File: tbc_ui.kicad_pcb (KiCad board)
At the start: 2 copper layers, 160 x 50 mm, 30 parts, among them J1 75869-105LF, SW1 PEC11R-4220F-S0024, U1 CD74HC14M96

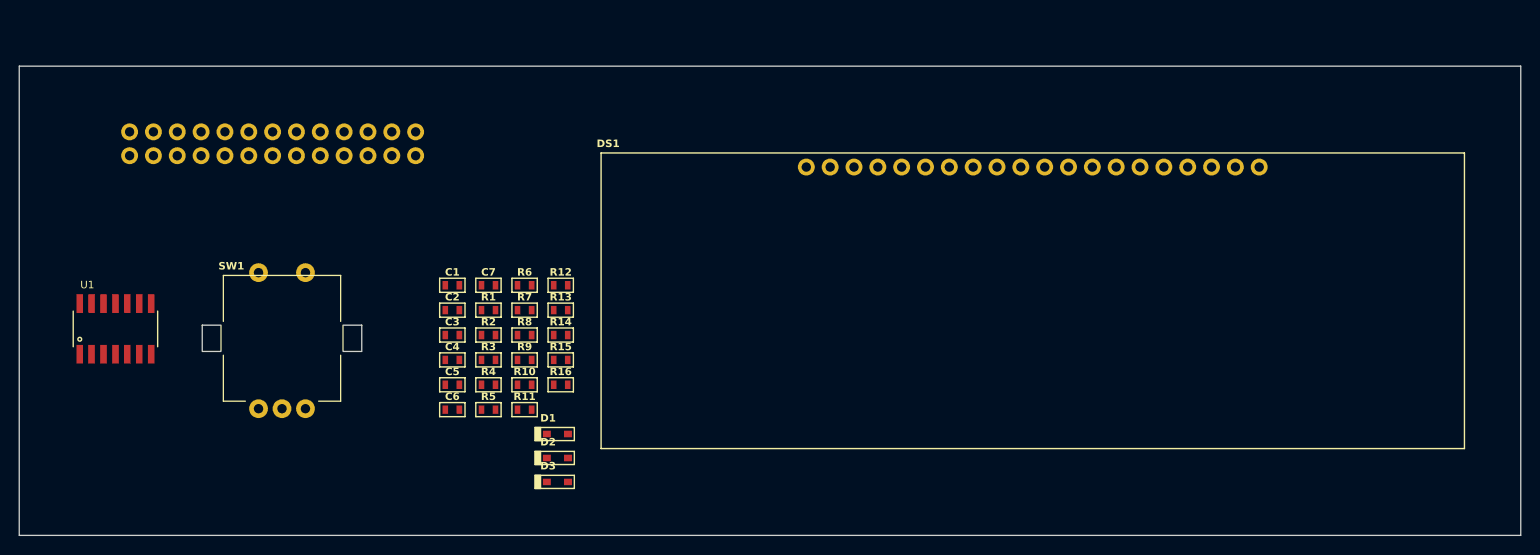
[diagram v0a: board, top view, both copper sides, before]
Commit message: additional footprints and layout
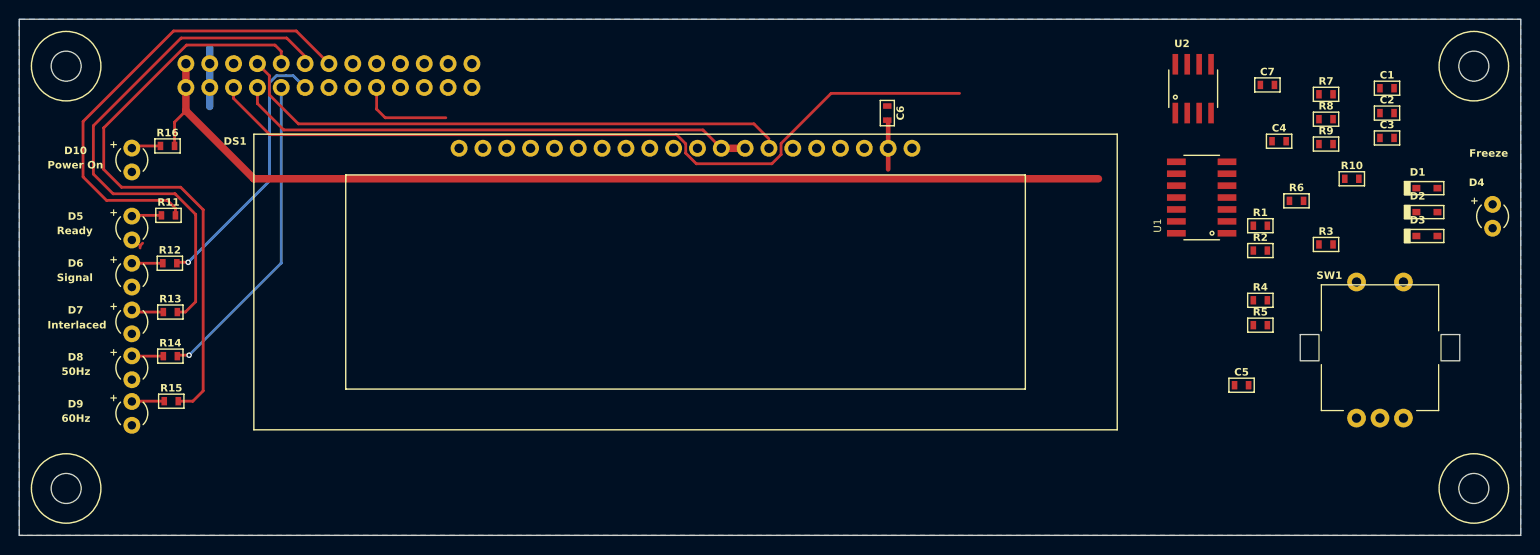
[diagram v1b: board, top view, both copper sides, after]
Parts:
- added D10: WP424NDT, tbc-ui:WP424, F.Cu at (92.0, 80.0)
- added D4: WP424IDT, tbc-ui:WP424, F.Cu at (237.0, 86.0)
- added D5: WP424GDT, tbc-ui:WP424, F.Cu at (92.0, 87.2)
- added D6: WP424GDT, tbc-ui:WP424, F.Cu at (92.0, 92.3)
- added D7: WP424GDT, tbc-ui:WP424, F.Cu at (92.0, 97.2)
- added D8: WP424GDT, tbc-ui:WP424, F.Cu at (92.0, 102.1)
- added D9: WP424GDT, tbc-ui:WP424, F.Cu at (92.0, 107.0)
- added MH1: MH_7.4MMNCx3.2MMD, tbc-ui:MH_7.4MMCx3.2MMD_NON_COPPER_NPTH, F.Cu at (85.0, 70.0)
- added MH2: MH_7.4MMNCx3.2MMD, tbc-ui:MH_7.4MMCx3.2MMD_NON_COPPER_NPTH, F.Cu at (85.0, 115.0)
- added MH3: MH_7.4MMNCx3.2MMD, tbc-ui:MH_7.4MMCx3.2MMD_NON_COPPER_NPTH, F.Cu at (235.0, 70.0)
- added MH4: MH_7.4MMNCx3.2MMD, tbc-ui:MH_7.4MMCx3.2MMD_NON_COPPER_NPTH, F.Cu at (235.0, 115.0)
- added U2: ICM7555CBAZ, tbc-ui:SOIC-8, F.Cu at (205.1, 72.4)
- moved SW1 117.0 mm to (225.0, 100.0)
- moved U1 116.6 mm to (206.0, 84.0), turned to 90 degrees
- moved C1 101.8 mm to (225.8, 72.3)
- moved C2 101.8 mm to (225.8, 75.0)
- moved C3 101.8 mm to (225.8, 77.7)
- moved D1 96.3 mm to (230.0, 83.0)
- moved D2 96.3 mm to (230.0, 85.5)
- moved D3 96.3 mm to (230.0, 88.1)
- moved C4 91.1 mm to (214.2, 78.0)
- moved R10 90.8 mm to (222.0, 82.0)
- moved R3 90.1 mm to (219.2, 89.0)
- moved R7 88.4 mm to (219.2, 73.0)
- moved R8 88.4 mm to (219.2, 75.7)
- moved R9 88.4 mm to (219.2, 78.3)
- moved C7 85.7 mm to (213.0, 72.0)
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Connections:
- DS1 pad 1: (no net) -> GND
- DS1 pad 10: (no net) -> GND
- DS1 pad 11: (no net) -> GND
- DS1 pad 12: (no net) -> GND
- DS1 pad 13: (no net) -> GND
- DS1 pad 14: (no net) -> GND
- DS1 pad 15: (no net) -> GND
- DS1 pad 16: (no net) -> +3V3
- DS1 pad 17: (no net) -> GND
- DS1 pad 18: (no net) -> +3V3
- DS1 pad 19: (no net) -> GND
- DS1 pad 2: (no net) -> +3V3
- DS1 pad 20: (no net) -> GND
- DS1 pad 3: (no net) -> GND
- DS1 pad 4: (no net) -> GND
- DS1 pad 5: (no net) -> GND
- DS1 pad 6: (no net) -> GND
- DS1 pad 7: (no net) -> /SCL
- DS1 pad 8: (no net) -> /SDA
- DS1 pad 9: (no net) -> /SDA
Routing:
- net +3V3: track 0.00 -> 115.2 mm
- net /FREEZE: track 0.00 -> 85.8 mm
- net /D_60HZ: track 0.00 -> 63.4 mm
- net /SCL: track 0.00 -> 59.0 mm
- net /D_INTERLACED: track 0.00 -> 58.2 mm
- net /SDA: track 0.00 -> 55.7 mm
- net /D_READY: track 0.00 -> 49.5 mm
- net /D_50HZ: track 0.00 -> 33.9 mm, vias 0 -> 1
- net /D_SIGNAL: track 0.00 -> 28.6 mm, vias 0 -> 1
- net /RENC_B: track 0.00 -> 10.1 mm
- net GND: track 0.00 -> 6.25 mm
- net Net-(D9-Anode): track 0.00 -> 3.46 mm
- net Net-(D7-Anode): track 0.00 -> 3.44 mm
- net Net-(D8-Anode): track 0.00 -> 3.36 mm
- net Net-(D6-Anode): track 0.00 -> 3.30 mm
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- added copper zone on B.Cu, net GND
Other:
- board size 160 x 50 mm -> 160 x 55 mm

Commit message: updated to Kicad 8, finished footprints and layouts, erc passed
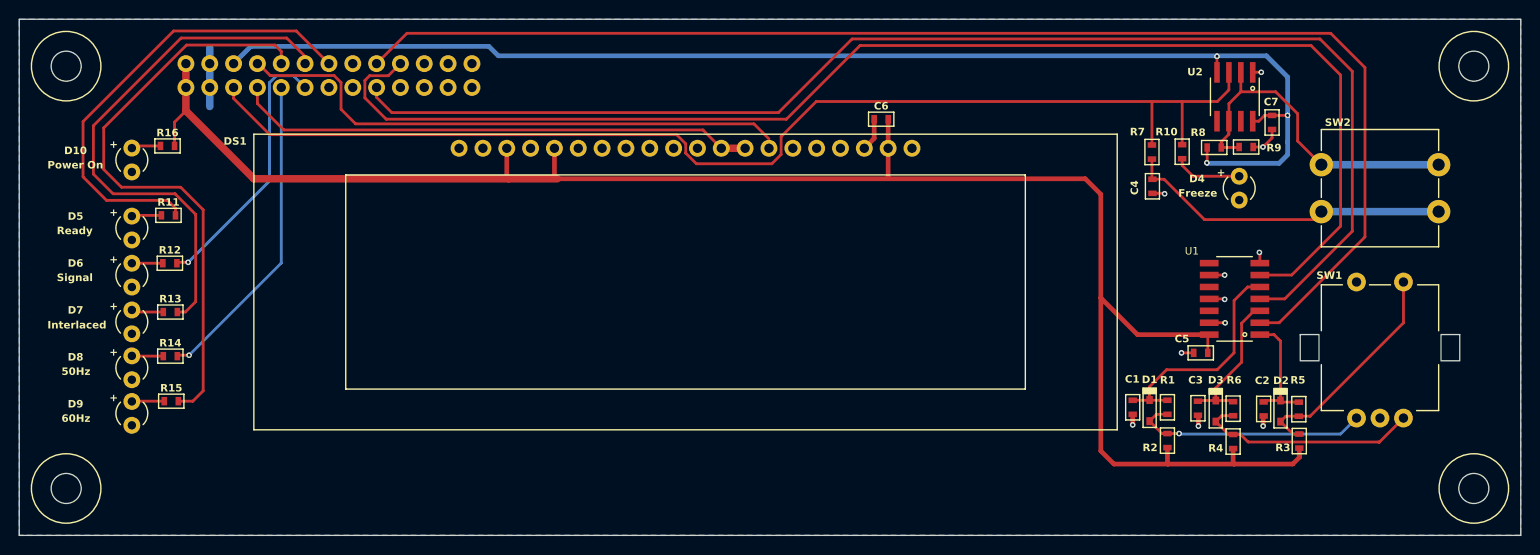
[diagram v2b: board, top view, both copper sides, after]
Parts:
- added SW2: TL1100F160Q, tbc-ui:TL1100F, F.Cu at (225.0, 83.0)
- moved C1 43.5 mm to (198.7, 106.3), turned to 90 degrees
- moved D1 37.9 mm to (200.4, 106.7), turned to -90 degrees
- moved C3 35.1 mm to (205.6, 106.5), turned to 90 degrees
- moved C2 34.2 mm to (212.6, 106.5), turned to 90 degrees
- moved D3 29.2 mm to (207.5, 106.8), turned to -90 degrees
- moved D4 27.2 mm to (210.0, 83.0)
- moved D2 26.3 mm to (214.4, 106.8), turned to -90 degrees
- moved R6 23.2 mm to (209.3, 106.5), turned to -90 degrees
- moved R2 22.5 mm to (202.3, 109.9), turned to 90 degrees
- moved R1 21.7 mm to (202.3, 106.3), turned to -90 degrees
- moved R3 21.1 mm to (216.4, 110.0), turned to -90 degrees
- moved R7 19.5 mm to (200.7, 79.2), turned to 90 degrees
- moved R10 18.3 mm to (203.9, 79.1), turned to 90 degrees
- moved R4 15.3 mm to (209.3, 110.0), turned to -90 degrees
- moved C4 14.3 mm to (200.8, 82.8), turned to 90 degrees
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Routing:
- net /RENC_A: track 0.00 -> 142.7 mm
- net /RENC_SW: track 0.00 -> 141.2 mm
- net +5V: track 0.00 -> 139.1 mm, vias 0 -> 3
- net /RENC_B: track 10.1 -> 140.3 mm
- net +3V3: track 115.2 -> 192.9 mm
- net /FREEZE: track 85.8 -> 126.2 mm
- net Net-(U2-THR): track 0.00 -> 37.0 mm
- net Net-(C4-Pad2): track 0.00 -> 34.8 mm
- net Net-(D1-A): track 0.00 -> 25.5 mm, vias 0 -> 1
- net Net-(D1-K): track 0.00 -> 24.6 mm
- net Net-(D2-A): track 0.00 -> 24.4 mm
- net Net-(D3-A): track 0.00 -> 24.1 mm
- net GND: track 6.25 -> 26.2 mm, vias 0 -> 11
- net Net-(D3-K): track 0.00 -> 15.7 mm
- net Net-(D2-K): track 0.00 -> 12.7 mm
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
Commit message: added gerbers and drills
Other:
- board text added: "Time Base Corrector and Scaler - UI https://github.com/philmcm/tbc_ui Version ${VERSION}"
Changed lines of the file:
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@@
 			(plot_on_all_layers_selection 0x0000000_00000000)
 			(disableapertmacros no)
-			(usegerberextensions no)
+			(usegerberextensions yes)
 			(usegerberattributes yes)
 			(usegerberadvancedattributes yes)
-			(creategerberjobfile yes)
+			(creategerberjobfile no)
 			(dashed_line_dash_ratio 12.000000)
 			(dashed_line_gap_ratio 3.000000)
@@
 			(outputformat 1)
 			(mirror no)
-			(drillshape 1)
+			(drillshape 0)
 			(scaleselection 1)
-			(outputdirectory "")
+			(outputdirectory "gerbers/")
 		)
 	)
+	(property "VERSION" "1")
 	(net 0 "")
 	(net 1 "GND")
@@
 		)
 		(property "Value" "560"
-			(at 0 1.55 270)
+			(at 0 1.55 -90)
 			(layer "F.Fab")
 			(hide yes)
@@
 		)
 		(property "Mouser" "603-RC0603FR-07560RL"
-			(at 0 0 270)
+			(at 0 0 -90)
 			(layer "F.Fab")
 			(hide yes)
@@
 		)
 		(fp_text user "${REFERENCE}"
-			(at 0 0 270)
+			(at 0 0 -90)
 			(layer "F.Fab")
 			(effects
@@
 		)
 		(property "Value" "0.01u"
-			(at 0 1.55 270)
+			(at 0 1.55 -90)
 			(layer "F.Fab")
 			(hide yes)
@@
 		)
 		(property "Mouser" " 81-GCM188R71H103KA7J"
-			(at 0 0 270)
+			(at 0 0 -90)
 			(layer "F.Fab")
 			(hide yes)
@@
 		)
 		(fp_text user "${REFERENCE}"
-			(at 0 0 270)
+			(at 0 0 -90)
 			(layer "F.Fab")
 			(effects
@@
 		(at 171.85 75.65)
 		(property "Reference" "C6"
-			(at 0 -1.4 360)
+			(at 0 -1.4 0)
 			(layer "F.SilkS")
 			(effects
@@
 		)
 		(property "Value" "100n"
-			(at 0 1.55 360)
+			(at 0 1.55 0)
 			(layer "F.Fab")
 			(hide yes)
@@
 		)
 		(fp_text user "${REFERENCE}"
-			(at 0 0 360)
+			(at 0 0 0)
 			(layer "F.Fab")
 			(effects
@@
 		(at 200.75 82.8 90)
 		(property "Reference" "C4"
-			(at -0.15 -1.9 270)
+			(at -0.15 -1.9 -90)
 			(layer "F.SilkS")
 			(effects
@@
 		)
 		(property "Value" "1u|25V"
-			(at 0 1.55 270)
+			(at 0 1.55 -90)
 			(layer "F.Fab")
 			(hide yes)
@@
 		)
 		(property "Mouser" " 81-GCJ188R71E105KA1D"
-			(at 0 0 270)
+			(at 0 0 -90)
 			(layer "F.Fab")
 			(hide yes)
@@
 		)
 		(fp_text user "${REFERENCE}"
-			(at 0 0 270)
+			(at 0 0 -90)
 			(layer "F.Fab")
 			(effects
@@
 		)
 		(property "Value" "100k"
-			(at 0 1.55 270)
+			(at 0 1.55 -90)
 			(layer "F.Fab")
 			(hide yes)
@@
 		)
 		(property "Mouser" " 603-RC0603FR-07100KL"
-			(at 0 0 270)
+			(at 0 0 -90)
 			(layer "F.Fab")
 			(hide yes)
@@
 		)
 		(fp_text user "${REFERENCE}"
-			(at 0 0 270)
+			(at 0 0 -90)
 			(layer "F.Fab")
 			(effects
@@
 		)
 		(property "Value" "0.01u"
-			(at 0 1.55 270)
+			(at 0 1.55 -90)
 			(layer "F.Fab")
 			(hide yes)
@@
 		)
 		(property "Mouser" " 81-GCM188R71H103KA7J"
-			(at 0 0 270)
+			(at 0 0 -90)
 			(layer "F.Fab")
 			(hide yes)
@@
 		)
 		(fp_text user "${REFERENCE}"
-			(at 0 0 270)
+			(at 0 0 -90)
 			(layer "F.Fab")
 			(effects
@@
 		)
 		(property "Value" "0.01u"
-			(at 0 1.55 270)
+			(at 0 1.55 -90)
 			(layer "F.Fab")
 			(hide yes)
@@
 		)
 		(property "Mouser" " 81-GCM188R71H103KA7J"
-			(at 0 0 270)
+			(at 0 0 -90)
 			(layer "F.Fab")
 			(hide yes)
@@
 		)
 		(fp_text user "${REFERENCE}"
-			(at 0 0 270)
+			(at 0 0 -90)
 			(layer "F.Fab")
 			(effects
@@
 		)
 		(property "Value" "100n"
-			(at 0 1.55 270)
+			(at 0 1.55 -90)
 			(layer "F.Fab")
 			(hide yes)
@@
 		)
 		(property "Mouser" " 81-GCJ188R71H104KA2D"
-			(at 0 0 270)
+			(at 0 0 -90)
 			(layer "F.Fab")
 			(hide yes)
@@
 		)
 		(fp_text user "${REFERENCE}"
-			(at 0 0 270)
+			(at 0 0 -90)
 			(layer "F.Fab")
 			(effects
@@
 		)
 		(property "Mouser" " 595-CD74HC14M96 "
-			(at 0 0 360)
+			(at 0 0 0)
 			(layer "F.Fab")
 			(hide yes)
@@
 		)
 		(property "Value" "10k"
-			(at 0 1.55 270)
+			(at 0 1.55 -90)
 			(layer "F.Fab")
 			(hide yes)
@@
 		)
 		(property "Mouser" "603-RC0603FR-0710KL"
-			(at 0 0 270)
+			(at 0 0 -90)
 			(layer "F.Fab")
 			(hide yes)
@@
 		)
 		(fp_text user "${REFERENCE}"
-			(at 0 0 270)
+			(at 0 0 -90)
 			(layer "F.Fab")
 			(effects
@@
 		(layer "Edge.Cuts")
 	)
+	(gr_text "Time Base Corrector and Scaler - UI\nhttps://github.com/philmcm/tbc_ui\nVersion ${VERSION}"
+		(at 202.3 117 0)
+		(layer "Dwgs.User")
+		(effects
+			(font
+				(size 0.8 0.8)
+				(thickness 0.15)
+			)
+			(justify left bottom)
+		)
+	)
 	(dimension

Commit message: new copper pours
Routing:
- net /FREEZE: track 126.2 -> 128.5 mm
- net GND: track 26.2 -> 24.2 mm, vias 11 -> 71
- added copper zone on F.Cu, net GND
